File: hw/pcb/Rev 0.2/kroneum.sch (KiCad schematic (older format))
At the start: 20 parts, among them J1 USB_B_Micro, J2 SWD, SW1 Boot_Mode_Btn, SW2 Ctrl_One_Btn, SW3 Reset_Btn, SW4 Ctrl_Ten_Btn, U1 STM32F042F4Px

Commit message: hw: use tl3342 for control and reset buttons.
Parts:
- SW2, SW3, SW4: footprint Button_Switch_SMD:SW_SPST_PTS645 -> tl3342:tl3342
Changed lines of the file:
@@
 F 0 "SW2" H 6000 3685 50  0000 C CNN
 F 1 "Ctrl_One_Btn" H 6000 3594 50  0000 C CNN
-F 2 "Button_Switch_SMD:SW_SPST_PTS645" H 6000 3600 50  0001 C CNN
+F 2 "tl3342:tl3342" H 6000 3600 50  0001 C CNN
 F 3 "" H 6000 3600 50  0001 C CNN
 	1    6000 3400
@@
 F 0 "SW3" H 7250 3685 50  0000 C CNN
 F 1 "Reset_Btn" H 7250 3594 50  0000 C CNN
-F 2 "Button_Switch_SMD:SW_SPST_PTS645" H 7250 3600 50  0001 C CNN
+F 2 "tl3342:tl3342" H 7250 3600 50  0001 C CNN
 F 3 "" H 7250 3600 50  0001 C CNN
 	1    7250 3400
@@
 F 0 "SW4" H 8500 3685 50  0000 C CNN
 F 1 "Ctrl_Ten_Btn" H 8500 3594 50  0000 C CNN
-F 2 "Button_Switch_SMD:SW_SPST_PTS645" H 8500 3600 50  0001 C CNN
+F 2 "tl3342:tl3342" H 8500 3600 50  0001 C CNN
 F 3 "" H 8500 3600 50  0001 C CNN
 	1    8500 3400

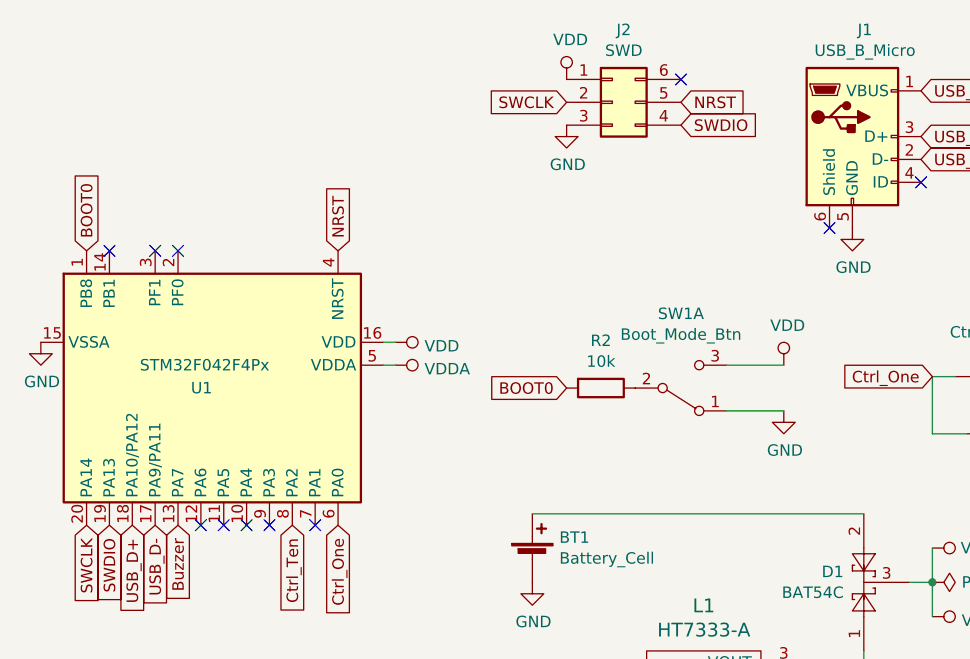
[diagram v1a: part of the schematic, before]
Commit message: hw: use momentary switch for boot mode selector.
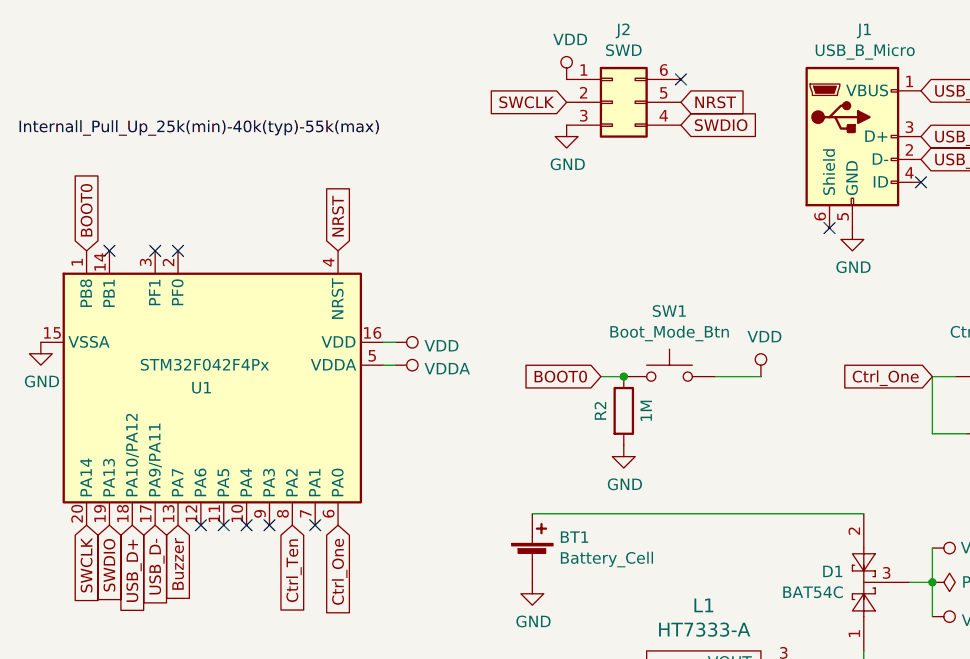
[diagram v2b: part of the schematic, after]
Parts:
- removed SW1: Boot_Mode_Btn, Button_Switch_SMD:SW_SPST_PTS645, symbol Switch:SW_DPDT_x2
- added SW1: Boot_Mode_Btn, tl3342:tl3342, symbol Switch:SW_Push
- BT1: footprint Battery:BatteryHolder_Keystone_103_1x20mm -> Battery:BatteryHolder_LINX_BAT-HLD-012-SMT
- R2: value 10k -> 1M
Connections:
- net BOOT0: now also R2.1, SW1.1; no longer R2.2
- net GND: now also R2.2
- net VDD: now also SW1.2
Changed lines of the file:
@@
 BOOT0
-$Comp
-L Device:R R2
-U 1 1 5C20BB63
-P 4250 3450
-F 0 "R2" V 4043 3450 50  0000 C CNN
-F 1 "10k" V 4134 3450 50  0000 C CNN
-F 2 "Resistor_SMD:R_0805_2012Metric_Pad1.15x1.40mm_HandSolder" V 4180 3450 50  0001 C CNN
-F 3 "~" H 4250 3450 50  0001 C CNN
-	1    4250 3450
-	0    1    1    0
-$EndComp
-$Comp
-L Switch:SW_DPDT_x2 SW1
-U 1 1 5C20BDA0
-P 4600 3450
-F 0 "SW1" H 4600 3125 50  0000 C CNN
-F 1 "Boot_Mode_Btn" H 4600 3216 50  0000 C CNN
-F 2 "Button_Switch_SMD:SW_SPST_PTS645" H 4600 3450 50  0001 C CNN
-F 3 "" H 4600 3450 50  0001 C CNN
-	1    4600 3450
-	1    0    0    1
-$EndComp
-Wire Wire Line
-	4800 3550 5050 3550
 $Comp
 L power:GND #PWR020
 U 1 1 5C20CB7E
-P 5050 3550
-F 0 "#PWR020" H 5050 3300 50  0001 C CNN
-F 1 "GND" H 5055 3377 50  0000 C CNN
-F 2 "" H 5050 3550 50  0001 C CNN
-F 3 "" H 5050 3550 50  0001 C CNN
-	1    5050 3550
-	1    0    0    -1
-$EndComp
-Wire Wire Line
-	4800 3350 5050 3350
-Text GLabel 4100 3450 0    50   Input ~ 0
+P 4350 3700
+F 0 "#PWR020" H 4350 3450 50  0001 C CNN
+F 1 "GND" H 4355 3527 50  0000 C CNN
+F 2 "" H 4350 3700 50  0001 C CNN
+F 3 "" H 4350 3700 50  0001 C CNN
+	1    4350 3700
+	1    0    0    -1
+$EndComp
+Text GLabel 4250 3400 0    50   Input ~ 0
 BOOT0
 Text GLabel 3100 4050 3    50   Input ~ 0
@@
 L power:VDD #PWR0102
 U 1 1 5C2140A0
-P 5050 3350
-F 0 "#PWR0102" H 5050 3200 50  0001 C CNN
-F 1 "VDD" H 5067 3523 50  0000 C CNN
-F 2 "" H 5050 3350 50  0001 C CNN
-F 3 "" H 5050 3350 50  0001 C CNN
-	1    5050 3350
+P 4950 3400
+F 0 "#PWR0102" H 4950 3250 50  0001 C CNN
+F 1 "VDD" H 4967 3573 50  0000 C CNN
+F 2 "" H 4950 3400 50  0001 C CNN
+F 3 "" H 4950 3400 50  0001 C CNN
+	1    4950 3400
 	1    0    0    -1
 $EndComp
@@
 F 0 "BT1" H 4068 4296 50  0000 L CNN
 F 1 "Battery_Cell" H 4068 4205 50  0000 L CNN
-F 2 "Battery:BatteryHolder_Keystone_103_1x20mm" V 3950 4260 50  0001 C CNN
+F 2 "Battery:BatteryHolder_LINX_BAT-HLD-012-SMT" V 3950 4260 50  0001 C CNN
 F 3 "~" V 3950 4260 50  0001 C CNN
 	1    3950 4200
@@
 NoConn ~ 2300 2850
 NoConn ~ 2400 2850
+$Comp
+L Switch:SW_Push SW1
+U 1 1 5C424334
+P 4550 3400
+F 0 "SW1" H 4550 3685 50  0000 C CNN
+F 1 "Boot_Mode_Btn" H 4550 3594 50  0000 C CNN
+F 2 "tl3342:tl3342" H 4550 3600 50  0001 C CNN
+F 3 "" H 4550 3600 50  0001 C CNN
+	1    4550 3400
+	1    0    0    -1
+$EndComp
+$Comp
+L Device:R R2
+U 1 1 5C4250E3
+P 4350 3550
+F 0 "R2" V 4250 3550 50  0000 C CNN
+F 1 "1M" V 4450 3550 50  0000 C CNN
+F 2 "Resistor_SMD:R_0805_2012Metric_Pad1.15x1.40mm_HandSolder" V 4280 3550 50  0001 C CNN
+F 3 "~" H 4350 3550 50  0001 C CNN
+	1    4350 3550
+	1    0    0    -1
+$EndComp
+Wire Wire Line
+	4250 3400 4350 3400
+Connection ~ 4350 3400
+Wire Wire Line
+	4750 3400 4950 3400
+Text Label 1700 2350 0    50   ~ 0
+Internall_Pull_Up_25k(min)-40k(typ)-55k(max)
 $EndSCHEMATC

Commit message: hw: provide footprint for SWD header.
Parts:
- J2: footprint (none) -> Connector_PinSocket_1.27mm:PinSocket_2x03_P1.27mm_Vertical_SMD
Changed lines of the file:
@@
 F 0 "J2" H 4350 2517 50  0000 C CNN
 F 1 "SWD" H 4350 2426 50  0000 C CNN
-F 2 "" H 4300 2200 50  0001 C CNN
+F 2 "Connector_PinSocket_1.27mm:PinSocket_2x03_P1.27mm_Vertical_SMD" H 4300 2200 50  0001 C CNN
 F 3 "~" H 4300 2200 50  0001 C CNN
 	1    4300 2200

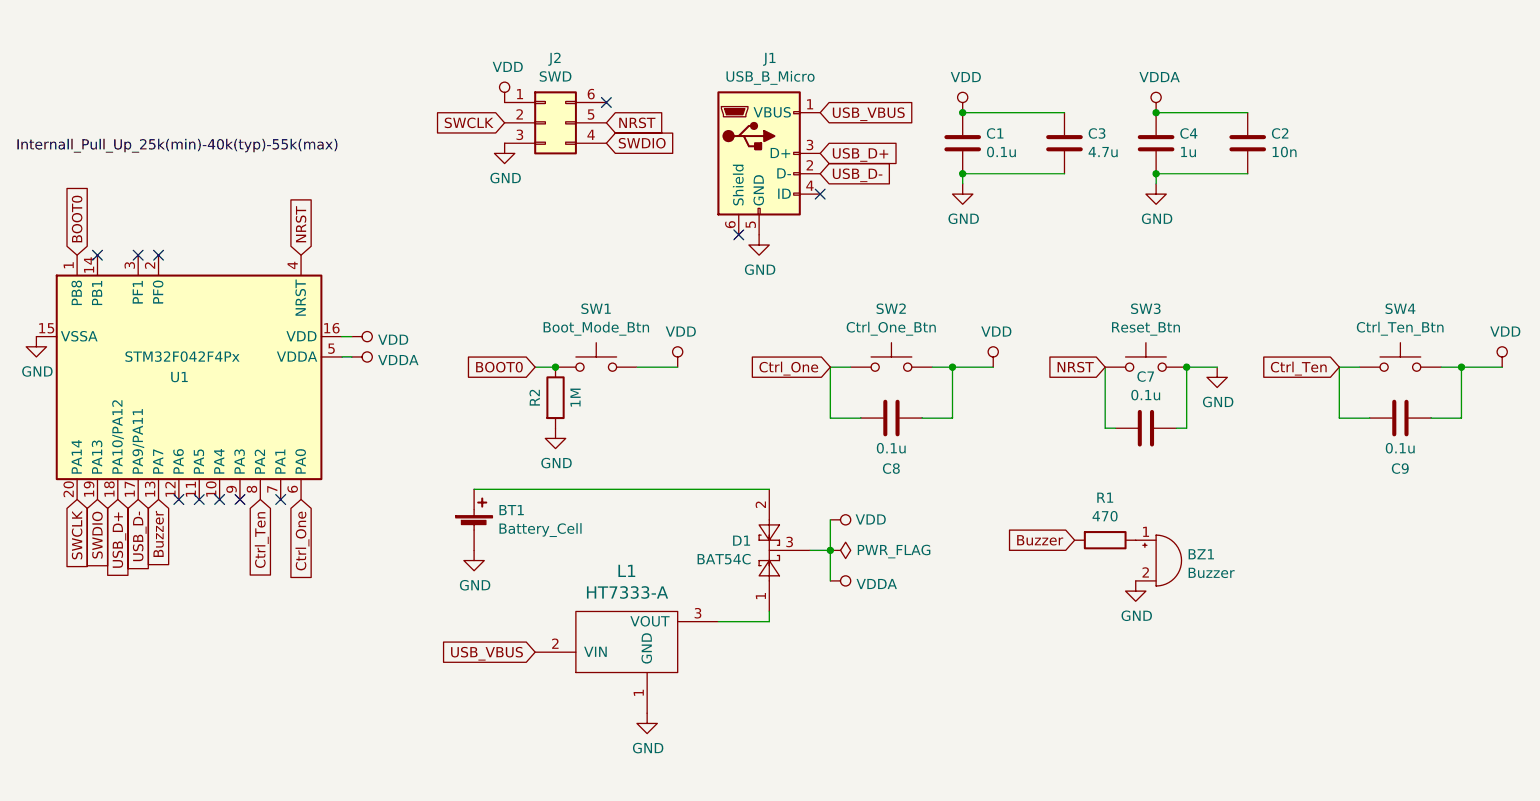
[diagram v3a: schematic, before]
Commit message: hw: reorganize headers on PCB.
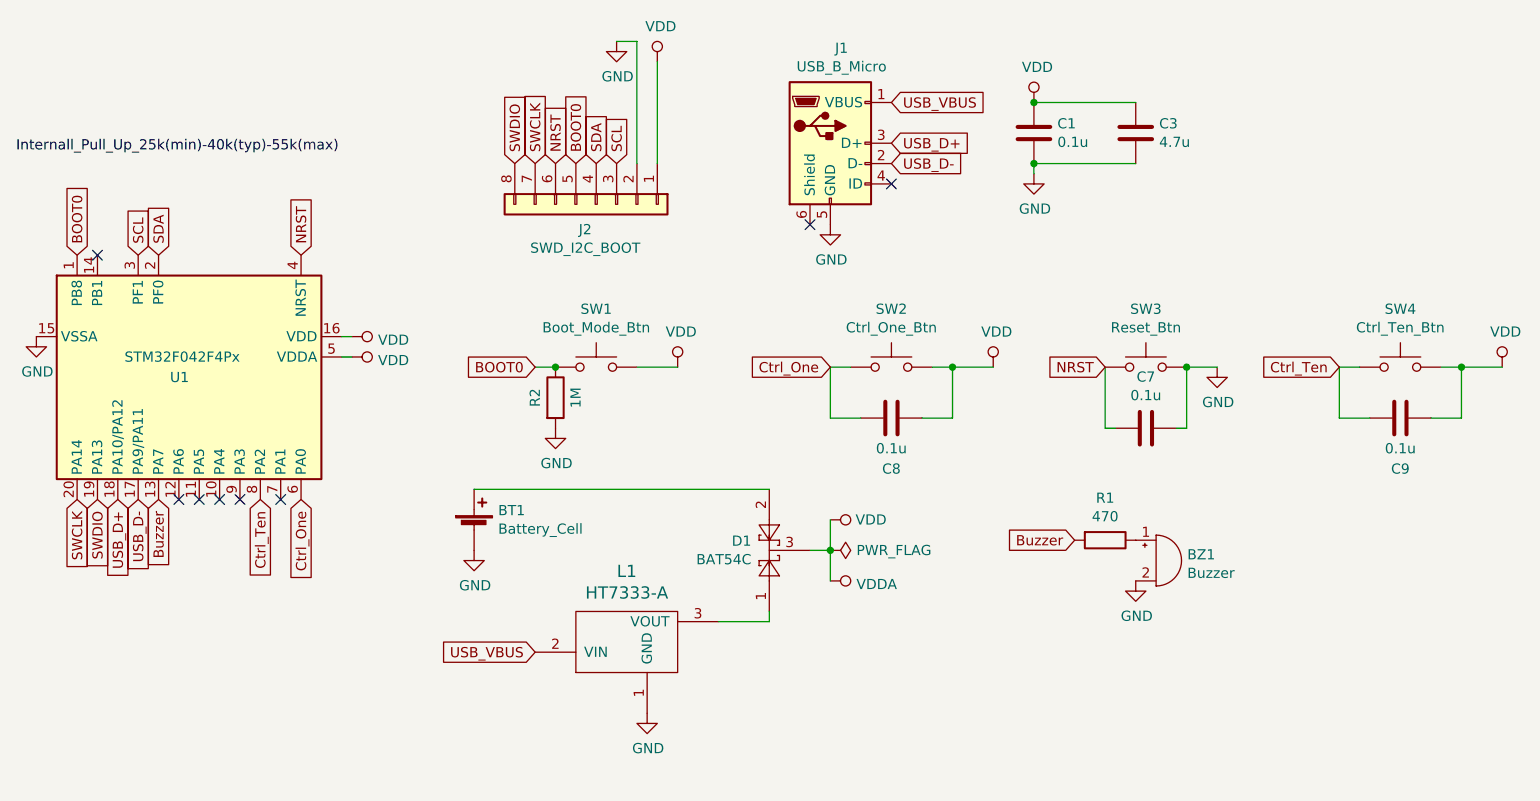
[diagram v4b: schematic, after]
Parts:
- removed C2: 10n, Capacitor_SMD:C_0805_2012Metric_Pad1.15x1.40mm_HandSolder, symbol Device:C
- removed C4: 1u, Capacitor_SMD:C_0805_2012Metric_Pad1.15x1.40mm_HandSolder, symbol Device:C
- removed J2: SWD, Connector_PinSocket_1.27mm:PinSocket_2x03_P1.27mm_Vertical_SMD, symbol Connector_Generic:Conn_02x03_Counter_Clockwise
- added J2: SWD_I2C_BOOT, Connector_PinSocket_2.54mm:PinSocket_1x08_P2.54mm_Vertical, symbol Connector_Generic:Conn_01x08
- J1: footprint Connector_USB:USB_Micro-B_Molex-105017-0001 -> micro_usb:USB_Micro-B_Molex-105017-0001
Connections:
- net BOOT0: now also J2.5 (Pin_5)
- net GND: now also J2.2 (Pin_2)
- net NRST: now also J2.6 (Pin_6)
- net SWCLK: now also J2.7 (Pin_7)
- net SWDIO: now also J2.8 (Pin_8)
- net VDD: now also J2.1 (Pin_1)
- net SDA: now reaches U1.2 (PF0)
- net SDA: now also J2.4 (Pin_4)
- net SCL: now reaches U1.3 (PF1)
- net SCL: now also J2.3 (Pin_3)
- no-connect marks 11 -> 8
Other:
- moved on the sheet: C1, C3, J1
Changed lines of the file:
@@
 L Connector:USB_B_Micro J1
 U 1 1 5C1E9F15
-P 5350 2350
-F 0 "J1" H 5405 2817 50  0000 C CNN
-F 1 "USB_B_Micro" H 5405 2726 50  0000 C CNN
-F 2 "Connector_USB:USB_Micro-B_Molex-105017-0001" H 5500 2300 50  0001 C CNN
-F 3 "~" H 5500 2300 50  0001 C CNN
-	1    5350 2350
-	1    0    0    -1
-$EndComp
-$Comp
-L Device:C C4
-U 1 1 5C1EC1E3
-P 7300 2300
-F 0 "C4" H 7415 2346 50  0000 L CNN
-F 1 "1u" H 7415 2255 50  0000 L CNN
-F 2 "Capacitor_SMD:C_0805_2012Metric_Pad1.15x1.40mm_HandSolder" H 7338 2150 50  0001 C CNN
-F 3 "~" H 7300 2300 50  0001 C CNN
-	1    7300 2300
-	1    0    0    -1
-$EndComp
-$Comp
-L Device:C C2
-U 1 1 5C1EC257
-P 7750 2300
-F 0 "C2" H 7865 2346 50  0000 L CNN
-F 1 "10n" H 7865 2255 50  0000 L CNN
-F 2 "Capacitor_SMD:C_0805_2012Metric_Pad1.15x1.40mm_HandSolder" H 7788 2150 50  0001 C CNN
-F 3 "~" H 7750 2300 50  0001 C CNN
-	1    7750 2300
-	1    0    0    -1
-$EndComp
-$Comp
-L power:GND #PWR06
-U 1 1 5C1EC59B
-P 7300 2500
-F 0 "#PWR06" H 7300 2250 50  0001 C CNN
-F 1 "GND" H 7305 2327 50  0000 C CNN
-F 2 "" H 7300 2500 50  0001 C CNN
-F 3 "" H 7300 2500 50  0001 C CNN
-	1    7300 2500
+P 5700 2300
+F 0 "J1" H 5755 2767 50  0000 C CNN
+F 1 "USB_B_Micro" H 5755 2676 50  0000 C CNN
+F 2 "micro_usb:USB_Micro-B_Molex-105017-0001" H 5850 2250 50  0001 C CNN
+F 3 "~" H 5850 2250 50  0001 C CNN
+	1    5700 2300
 	1    0    0    -1
 $EndComp
 Wire Wire Line
 	3300 3250 3350 3250
-NoConn ~ 5650 2550
-NoConn ~ 5250 2750
+NoConn ~ 6000 2500
+NoConn ~ 5600 2700
 $Comp
 L power:GND #PWR01
 U 1 1 5C1EDFBA
-P 5350 2750
-F 0 "#PWR01" H 5350 2500 50  0001 C CNN
-F 1 "GND" H 5355 2577 50  0000 C CNN
-F 2 "" H 5350 2750 50  0001 C CNN
-F 3 "" H 5350 2750 50  0001 C CNN
-	1    5350 2750
+P 5700 2700
+F 0 "#PWR01" H 5700 2450 50  0001 C CNN
+F 1 "GND" H 5705 2527 50  0000 C CNN
+F 2 "" H 5700 2700 50  0001 C CNN
+F 3 "" H 5700 2700 50  0001 C CNN
+	1    5700 2700
 	1    0    0    -1
 $EndComp
@@
 $EndComp
 $Comp
-L power:VDDA #PWR015
-U 1 1 5C2010A1
-P 7300 2150
-F 0 "#PWR015" H 7300 2000 50  0001 C CNN
-F 1 "VDDA" H 7317 2323 50  0000 C CNN
-F 2 "" H 7300 2150 50  0001 C CNN
-F 3 "" H 7300 2150 50  0001 C CNN
-	1    7300 2150
-	1    0    0    -1
-$EndComp
-Wire Wire Line
-	7300 2500 7300 2450
-Connection ~ 7300 2150
-Connection ~ 7300 2450
-$Comp
-L power:VDDA #PWR04
-U 1 1 5C202694
-P 3350 3350
-F 0 "#PWR04" H 3350 3200 50  0001 C CNN
-F 1 "VDDA" V 3367 3478 50  0000 L CNN
-F 2 "" H 3350 3350 50  0001 C CNN
-F 3 "" H 3350 3350 50  0001 C CNN
-	1    3350 3350
-	0    1    1    0
-$EndComp
-$Comp
 L Device:C C1
 U 1 1 5C202927
-P 6350 2300
-F 0 "C1" H 6465 2346 50  0000 L CNN
-F 1 "0.1u" H 6465 2255 50  0000 L CNN
-F 2 "Capacitor_SMD:C_0805_2012Metric_Pad1.15x1.40mm_HandSolder" H 6388 2150 50  0001 C CNN
-F 3 "~" H 6350 2300 50  0001 C CNN
-	1    6350 2300
+P 6700 2250
+F 0 "C1" H 6815 2296 50  0000 L CNN
+F 1 "0.1u" H 6815 2205 50  0000 L CNN
+F 2 "Capacitor_SMD:C_0805_2012Metric_Pad1.15x1.40mm_HandSolder" H 6738 2100 50  0001 C CNN
+F 3 "~" H 6700 2250 50  0001 C CNN
+	1    6700 2250
 	1    0    0    -1
 $EndComp
@@
 L Device:C C3
 U 1 1 5C20292E
-P 6850 2300
-F 0 "C3" H 6965 2346 50  0000 L CNN
-F 1 "4.7u" H 6965 2255 50  0000 L CNN
-F 2 "Capacitor_SMD:C_0805_2012Metric_Pad1.15x1.40mm_HandSolder" H 6888 2150 50  0001 C CNN
-F 3 "~" H 6850 2300 50  0001 C CNN
-	1    6850 2300
+P 7200 2250
+F 0 "C3" H 7315 2296 50  0000 L CNN
+F 1 "4.7u" H 7315 2205 50  0000 L CNN
+F 2 "Capacitor_SMD:C_0805_2012Metric_Pad1.15x1.40mm_HandSolder" H 7238 2100 50  0001 C CNN
+F 3 "~" H 7200 2250 50  0001 C CNN
+	1    7200 2250
 	1    0    0    -1
 $EndComp
@@
 L power:GND #PWR08
 U 1 1 5C202935
-P 6350 2500
-F 0 "#PWR08" H 6350 2250 50  0001 C CNN
-F 1 "GND" H 6355 2327 50  0000 C CNN
-F 2 "" H 6350 2500 50  0001 C CNN
-F 3 "" H 6350 2500 50  0001 C CNN
-	1    6350 2500
-	1    0    0    -1
-$EndComp
-Wire Wire Line
-	6350 2500 6350 2450
-Connection ~ 6350 2450
-Wire Wire Line
-	7300 2150 7750 2150
-Wire Wire Line
-	7300 2450 7750 2450
-Wire Wire Line
-	6350 2150 6850 2150
-Wire Wire Line
-	6350 2450 6850 2450
+P 6700 2450
+F 0 "#PWR08" H 6700 2200 50  0001 C CNN
+F 1 "GND" H 6705 2277 50  0000 C CNN
+F 2 "" H 6700 2450 50  0001 C CNN
+F 3 "" H 6700 2450 50  0001 C CNN
+	1    6700 2450
+	1    0    0    -1
+$EndComp
+Wire Wire Line
+	6700 2450 6700 2400
+Connection ~ 6700 2400
+Wire Wire Line
+	6700 2100 7200 2100
+Wire Wire Line
+	6700 2400 7200 2400
 $Comp
 L power:VDD #PWR07
 U 1 1 5C203D31
-P 6350 2150
-F 0 "#PWR07" H 6350 2000 50  0001 C CNN
-F 1 "VDD" H 6367 2323 50  0000 C CNN
-F 2 "" H 6350 2150 50  0001 C CNN
-F 3 "" H 6350 2150 50  0001 C CNN
-	1    6350 2150
-	1    0    0    -1
-$EndComp
-Connection ~ 6350 2150
+P 6700 2100
+F 0 "#PWR07" H 6700 1950 50  0001 C CNN
+F 1 "VDD" H 6717 2273 50  0000 C CNN
+F 2 "" H 6700 2100 50  0001 C CNN
+F 3 "" H 6700 2100 50  0001 C CNN
+	1    6700 2100
+	1    0    0    -1
+$EndComp
+Connection ~ 6700 2100
 $Comp
 L power:VDD #PWR03
@@
 Text GLabel 2200 4050 3    50   Input ~ 0
 USB_D+
-Text GLabel 5650 2350 2    50   Input ~ 0
+Text GLabel 6000 2300 2    50   Input ~ 0
 USB_D+
-Text GLabel 5650 2450 2    50   Input ~ 0
+Text GLabel 6000 2400 2    50   Input ~ 0
 USB_D-
 $Comp
@@
 	1    0    0    -1
 $EndComp
-Text GLabel 5650 2150 2    50   Input ~ 0
+Text GLabel 6000 2100 2    50   Input ~ 0
 USB_VBUS
 $Comp
@@
 	1    0    0    -1
 $EndComp
-$Comp
-L Connector_Generic:Conn_02x03_Counter_Clockwise J2
-U 1 1 5C3E3D6A
-P 4300 2200
-F 0 "J2" H 4350 2517 50  0000 C CNN
-F 1 "SWD" H 4350 2426 50  0000 C CNN
-F 2 "Connector_PinSocket_1.27mm:PinSocket_2x03_P1.27mm_Vertical_SMD" H 4300 2200 50  0001 C CNN
-F 3 "~" H 4300 2200 50  0001 C CNN
-	1    4300 2200
-	1    0    0    -1
-$EndComp
-$Comp
-L power:VDD #PWR012
-U 1 1 5C3E417F
-P 4100 2100
-F 0 "#PWR012" H 4100 1950 50  0001 C CNN
-F 1 "VDD" H 4117 2273 50  0000 C CNN
-F 2 "" H 4100 2100 50  0001 C CNN
-F 3 "" H 4100 2100 50  0001 C CNN
-	1    4100 2100
-	1    0    0    -1
-$EndComp
-Text GLabel 4100 2200 0    50   Input ~ 0
-SWCLK
-$Comp
-L power:GND #PWR014
-U 1 1 5C3E423F
-P 4100 2300
-F 0 "#PWR014" H 4100 2050 50  0001 C CNN
-F 1 "GND" H 4105 2127 50  0000 C CNN
-F 2 "" H 4100 2300 50  0001 C CNN
-F 3 "" H 4100 2300 50  0001 C CNN
-	1    4100 2300
-	1    0    0    -1
-$EndComp
-Text GLabel 4600 2300 2    50   Input ~ 0
-SWDIO
-Text GLabel 4600 2200 2    50   Input ~ 0
-NRST
 Text GLabel 2000 4050 3    50   Input ~ 0
 SWCLK
 Text GLabel 2100 4050 3    50   Input ~ 0
 SWDIO
-NoConn ~ 4600 2100
-NoConn ~ 2300 2850
-NoConn ~ 2400 2850
 $Comp
 L Switch:SW_Push SW1
@@
 Text Label 1700 2350 0    50   ~ 0
 Internall_Pull_Up_25k(min)-40k(typ)-55k(max)
+$Comp
+L power:VDD #PWR0106
+U 1 1 5C4799FF
+P 3350 3350
+F 0 "#PWR0106" H 3350 3200 50  0001 C CNN
+F 1 "VDD" V 3367 3478 50  0000 L CNN
+F 2 "" H 3350 3350 50  0001 C CNN
+F 3 "" H 3350 3350 50  0001 C CNN
+	1    3350 3350
+	0    1    1    0
+$EndComp
+Text GLabel 2400 2850 1    50   Input ~ 0
+SDA
+Text GLabel 2300 2850 1    50   Input ~ 0
+SCL
+Text GLabel 4350 2400 1    50   Input ~ 0
+NRST
+Text GLabel 4250 2400 1    50   Input ~ 0
+SWCLK
+Text GLabel 4150 2400 1    50   Input ~ 0
+SWDIO
+Text GLabel 4650 2400 1    50   Input ~ 0
+SCL
+Text GLabel 4550 2400 1    50   Input ~ 0
+SDA
+Wire Wire Line
+	4750 2400 4750 1800
+$Comp
+L power:GND #PWR05
+U 1 1 5C4A8CEA
+P 4650 1800
+F 0 "#PWR05" H 4650 1550 50  0001 C CNN
+F 1 "GND" H 4655 1627 50  0000 C CNN
+F 2 "" H 4650 1800 50  0001 C CNN
+F 3 "" H 4650 1800 50  0001 C CNN
+	1    4650 1800
+	1    0    0    -1
+$EndComp
+$Comp
+L power:VDD #PWR04
+U 1 1 5C4A93B8
+P 4850 1900
+F 0 "#PWR04" H 4850 1750 50  0001 C CNN
+F 1 "VDD" H 4867 2073 50  0000 C CNN
+F 2 "" H 4850 1900 50  0001 C CNN
+F 3 "" H 4850 1900 50  0001 C CNN
+	1    4850 1900
+	1    0    0    -1
+$EndComp
+Wire Wire Line
+	4850 1900 4850 2400
+Wire Wire Line
+	4650 1800 4750 1800
+$Comp
+L Connector_Generic:Conn_01x08 J2
+U 1 1 5C4ADBE0
+P 4550 2600
+F 0 "J2" V 4674 2546 50  0000 C CNN
+F 1 "SWD_I2C_BOOT" V 4765 2546 50  0000 C CNN
+F 2 "Connector_PinSocket_2.54mm:PinSocket_1x08_P2.54mm_Vertical" H 4550 2600 50  0001 C CNN
+F 3 "~" H 4550 2600 50  0001 C CNN
+	1    4550 2600
+	0    1    1    0
+$EndComp
+Text GLabel 4450 2400 1    50   Input ~ 0
+BOOT0
 $EndSCHEMATC
